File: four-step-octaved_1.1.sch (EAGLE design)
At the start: 39 parts, among them IC1 556, IC2 4017N, IC3 4040N, J1 -BATTERY+, J2 SPEAKER, U1 LM386N

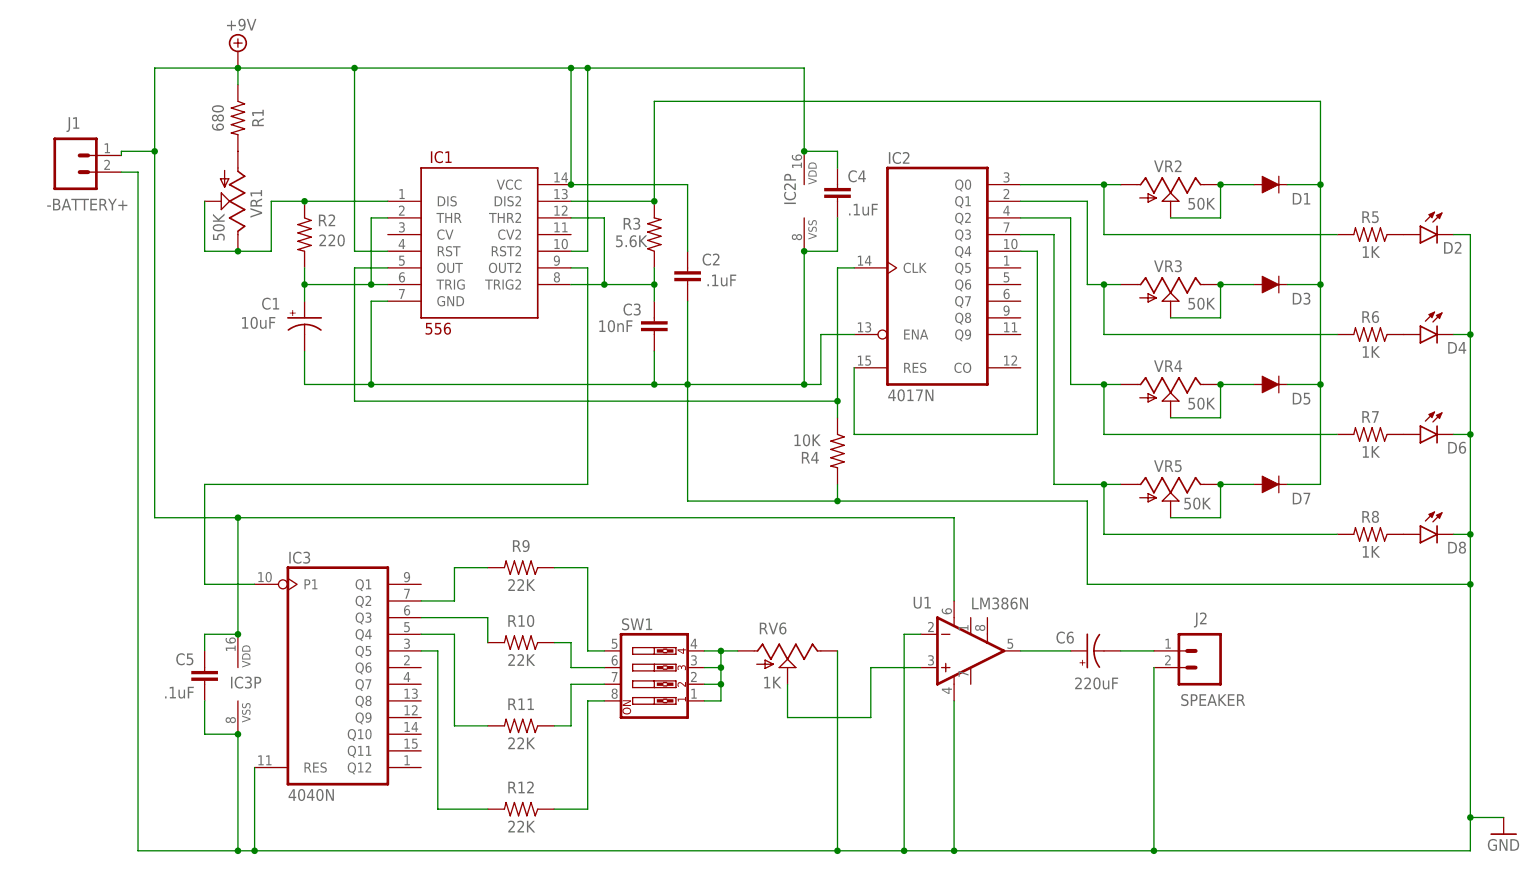
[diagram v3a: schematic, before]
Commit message: Add switch
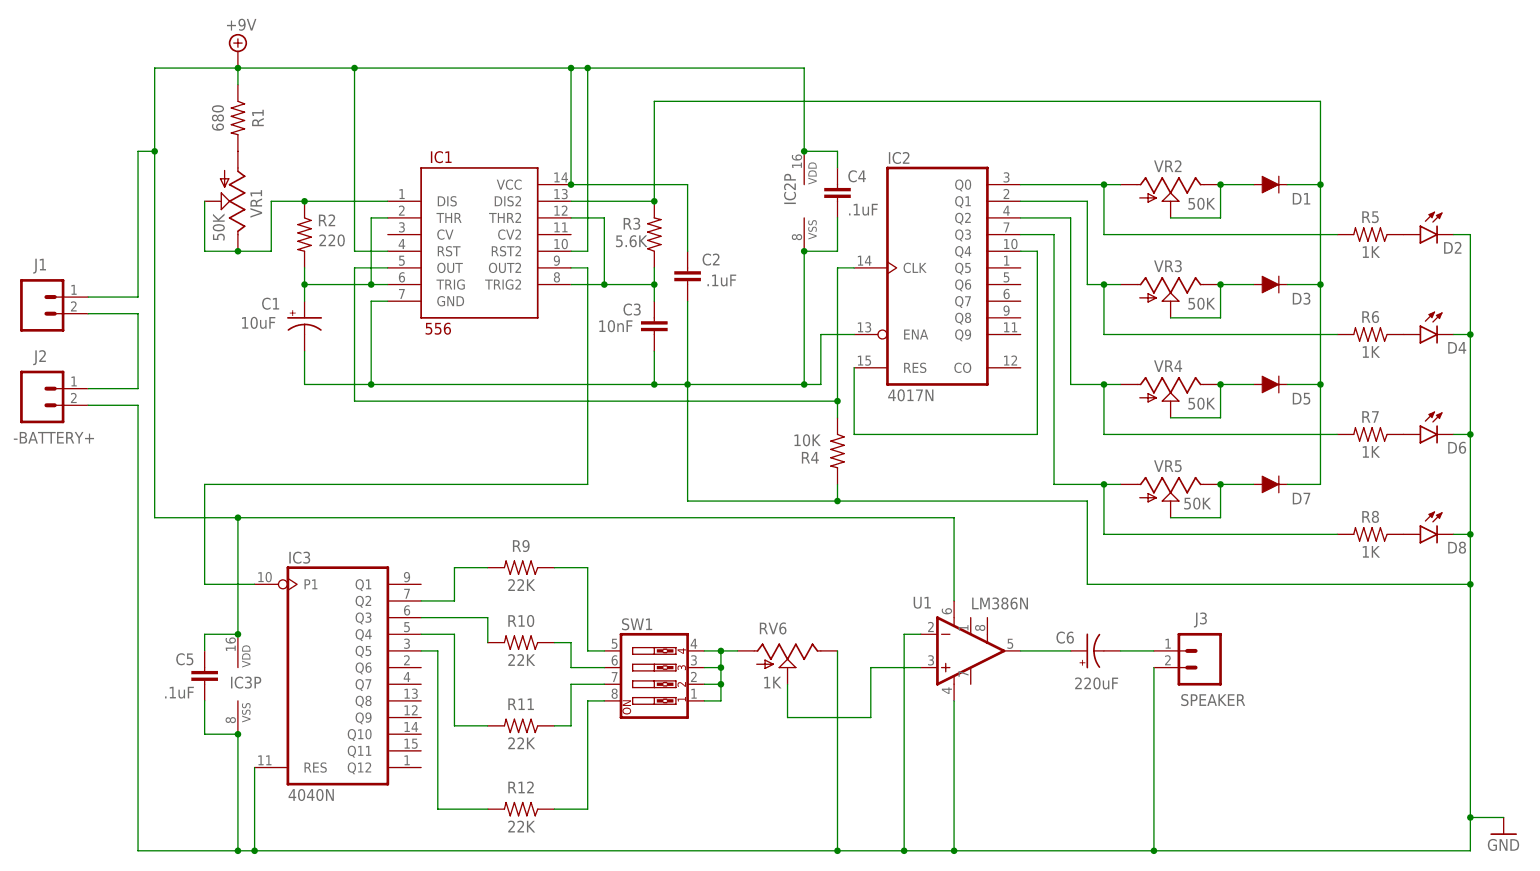
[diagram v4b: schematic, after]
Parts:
- added J3: SPEAKER, SparkFun-Connectors:CONN_02
- J1: value -BATTERY+ -> (none)
- J2: value SPEAKER -> -BATTERY+
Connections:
- new net N$32: J1.2, J2.1
- net GND: now also J3.2; no longer J1.2
- net N$27: now also J3.1; no longer J2.1
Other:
- moved on the sheet: J1, J2
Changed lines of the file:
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@@
 <setting verticaltext="up"/>
 </settings>
-<grid distance="0.1" unitdist="inch" unit="inch" style="lines" multiple="1" display="no" altdistance="0.01" altunitdist="inch" altunit="inch"/>
+<grid distance="0.025" unitdist="inch" unit="inch" style="lines" multiple="1" display="no" altdistance="0.01" altunitdist="inch" altunit="inch"/>
 <layers>
 <layer number="1" name="Top" color="4" fill="1" visible="no" active="no"/>
@@
 <part name="C5" library="SparkFun-Capacitors" deviceset="0.1UF" device="-KIT-EZ-50V-20%" value=".1uF"/>
 <part name="C6" library="SparkFun-Capacitors" deviceset="100UF-POLAR" device="-RADIAL-2.5MM-25V-20%" value="220uF"/>
-<part name="J2" library="SparkFun-Connectors" deviceset="CONN_02" device="" value="SPEAKER"/>
-<part name="J1" library="SparkFun-Connectors" deviceset="CONN_02" device="" value="-BATTERY+"/>
+<part name="J3" library="SparkFun-Connectors" deviceset="CONN_02" device="" value="SPEAKER"/>
+<part name="J2" library="SparkFun-Connectors" deviceset="CONN_02" device="" value="-BATTERY+"/>
 <part name="R11" library="SparkFun-Resistors" deviceset="1KOHM" device="-HORIZ-1/4W-1%" value="22K"/>
 <part name="R12" library="SparkFun-Resistors" deviceset="1KOHM" device="-HORIZ-1/4W-1%" value="22K"/>
 <part name="SW1" library="special" deviceset="SW_DIP-4" device=""/>
+<part name="J1" library="SparkFun-Connectors" deviceset="CONN_02" device=""/>
 </parts>
 <sheets>
@@
 <attribute name="VALUE" x="108.966" y="13.716" size="1.778" layer="96" font="vector" rot="R180"/>
 </instance>
-<instance part="J2" gate="G$1" x="121.92" y="17.78" smashed="yes" rot="R180">
+<instance part="J3" gate="G$1" x="121.92" y="17.78" smashed="yes" rot="R180">
 <attribute name="VALUE" x="128.27" y="11.176" size="1.778" layer="96" font="vector" rot="R180"/>
 <attribute name="NAME" x="122.555" y="23.622" size="1.778" layer="95" font="vector" rot="R180"/>
 </instance>
-<instance part="J1" gate="G$1" x="-50.8" y="93.345" smashed="yes" rot="MR180">
-<attribute name="VALUE" x="-54.61" y="86.741" size="1.778" layer="96" font="vector" rot="MR180"/>
-<attribute name="NAME" x="-51.435" y="99.187" size="1.778" layer="95" font="vector" rot="MR180"/>
+<instance part="J2" gate="G$1" x="-55.88" y="57.785" smashed="yes" rot="MR180">
+<attribute name="VALUE" x="-59.69" y="51.181" size="1.778" layer="96" font="vector" rot="MR180"/>
+<attribute name="NAME" x="-56.515" y="63.627" size="1.778" layer="95" font="vector" rot="MR180"/>
 </instance>
 <instance part="R11" gate="G$1" x="17.78" y="6.35" smashed="yes" rot="R180">
@@
 </instance>
 <instance part="SW1" gate="A" x="38.1" y="15.24"/>
+<instance part="J1" gate="G$1" x="-55.88" y="71.755" smashed="yes" rot="MR180">
+<attribute name="VALUE" x="-59.69" y="65.151" size="1.778" layer="96" font="vector" rot="MR180"/>
+<attribute name="NAME" x="-56.515" y="77.597" size="1.778" layer="95" font="vector" rot="MR180"/>
+</instance>
 </instances>
 <busses>
@@
 <wire x1="-30.48" y1="20.32" x2="-30.48" y2="17.78" width="0.1524" layer="91"/>
 <wire x1="-38.1" y1="106.68" x2="-38.1" y2="93.98" width="0.1524" layer="91"/>
-<pinref part="J1" gate="G$1" pin="1"/>
 <wire x1="-38.1" y1="93.98" x2="-38.1" y2="38.1" width="0.1524" layer="91"/>
-<wire x1="-38.1" y1="93.98" x2="-43.18" y2="93.98" width="0.1524" layer="91"/>
-<wire x1="-43.18" y1="93.98" x2="-43.18" y2="93.345" width="0.1524" layer="91"/>
+<wire x1="-38.1" y1="93.98" x2="-40.64" y2="93.98" width="0.1524" layer="91"/>
 <junction x="-38.1" y="93.98"/>
 <pinref part="IC1" gate="G$1" pin="RST2"/>
@@
 <wire x1="27.94" y1="78.74" x2="27.94" y2="106.68" width="0.1524" layer="91"/>
 <junction x="27.94" y="106.68"/>
+<pinref part="J1" gate="G$1" pin="1"/>
+<wire x1="-48.26" y1="71.755" x2="-40.64" y2="71.755" width="0.1524" layer="91"/>
+<wire x1="-40.64" y1="71.755" x2="-40.64" y2="93.98" width="0.1524" layer="91"/>
 </segment>
 </net>
@@
 <segment>
 <pinref part="C6" gate="G$1" pin="-"/>
-<pinref part="J2" gate="G$1" pin="1"/>
+<pinref part="J3" gate="G$1" pin="1"/>
 <wire x1="114.3" y1="17.78" x2="109.22" y2="17.78" width="0.1524" layer="91"/>
 </segment>
@@
 <wire x1="76.2" y1="-12.7" x2="83.82" y2="-12.7" width="0.1524" layer="91"/>
 <junction x="76.2" y="-12.7"/>
-<pinref part="J2" gate="G$1" pin="2"/>
+<pinref part="J3" gate="G$1" pin="2"/>
 <wire x1="114.3" y1="-12.7" x2="114.3" y2="15.24" width="0.1524" layer="91"/>
 <wire x1="83.82" y1="-12.7" x2="114.3" y2="-12.7" width="0.1524" layer="91"/>
@@
 <wire x1="104.14" y1="27.94" x2="104.14" y2="40.64" width="0.1524" layer="91"/>
 <junction x="162.56" y="27.94"/>
-<pinref part="J1" gate="G$1" pin="2"/>
-<wire x1="-43.18" y1="90.805" x2="-40.64" y2="90.805" width="0.1524" layer="91"/>
-<wire x1="-40.64" y1="90.805" x2="-40.64" y2="-12.7" width="0.1524" layer="91"/>
+<pinref part="J2" gate="G$1" pin="2"/>
+<wire x1="-48.26" y1="55.245" x2="-40.64" y2="55.245" width="0.1524" layer="91"/>
+<wire x1="-40.64" y1="55.245" x2="-40.64" y2="-12.7" width="0.1524" layer="91"/>
 <wire x1="-40.64" y1="-12.7" x2="-25.4" y2="-12.7" width="0.1524" layer="91"/>
 <junction x="-25.4" y="-12.7"/>
@@
 </segment>
 </net>
+<net name="N$32" class="0">
+<segment>
+<pinref part="J1" gate="G$1" pin="2"/>
+<wire x1="-48.26" y1="69.215" x2="-40.64" y2="69.215" width="0.1524" layer="91"/>
+<wire x1="-40.64" y1="69.215" x2="-40.64" y2="57.785" width="0.1524" layer="91"/>
+<pinref part="J2" gate="G$1" pin="1"/>
+<wire x1="-40.64" y1="57.785" x2="-48.26" y2="57.785" width="0.1524" layer="91"/>
+</segment>
+</net>

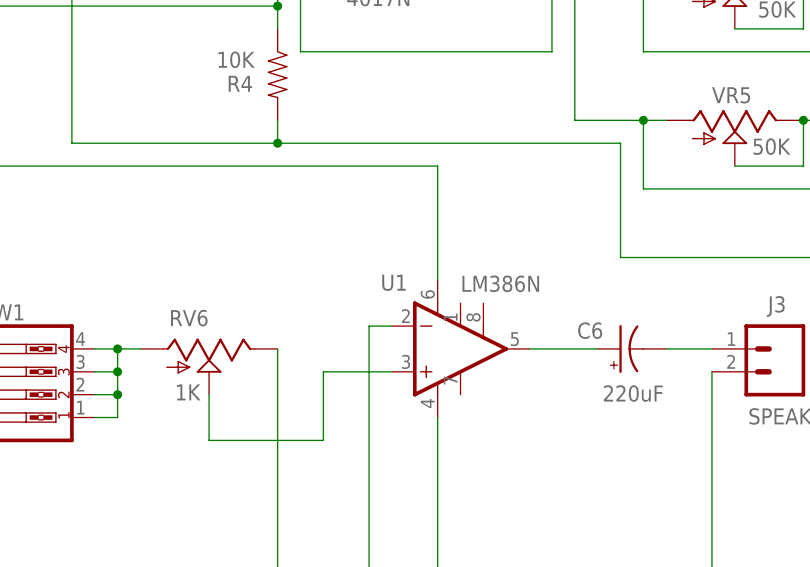
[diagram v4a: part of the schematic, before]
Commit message: Update 386 name
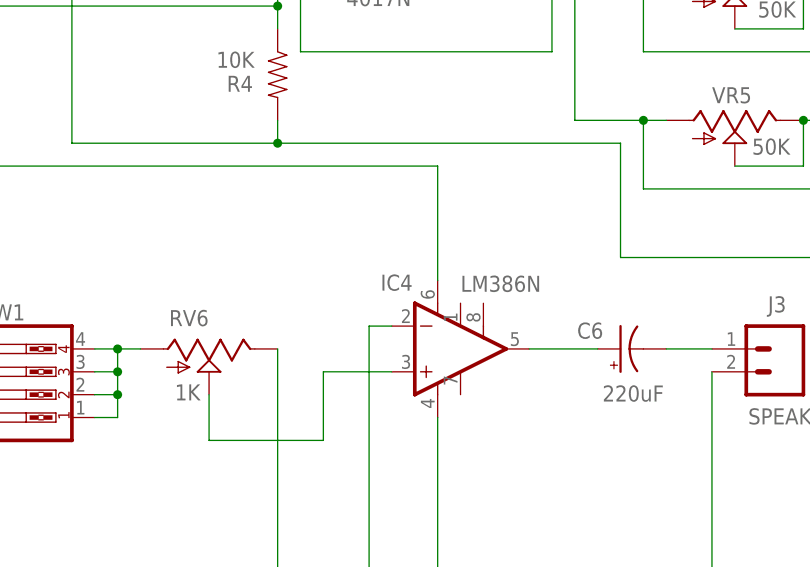
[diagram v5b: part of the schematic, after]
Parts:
- renumbered U1 to IC4
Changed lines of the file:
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@@
 <part name="IC2" library="40xx" deviceset="4017" device="N"/>
 <part name="IC3" library="40xx" deviceset="4040" device="N"/>
-<part name="U1" library="SparkFun-IC-Amplifiers" deviceset="LM386" device="" value="LM386N"/>
+<part name="IC4" library="SparkFun-IC-Amplifiers" deviceset="LM386" device="" value="LM386N"/>
 <part name="SUPPLY1" library="supply2" deviceset="+9V" device=""/>
 <part name="GND1" library="supply1" deviceset="GND" device=""/>
@@
 <instance part="IC2" gate="A" x="81.28" y="76.2"/>
 <instance part="IC3" gate="A" x="-10.16" y="15.24"/>
-<instance part="U1" gate="G1" x="83.82" y="17.78" smashed="yes">
+<instance part="IC4" gate="G1" x="83.82" y="17.78" smashed="yes">
 <attribute name="NAME" x="77.47" y="24.257" size="1.778" layer="95" font="vector"/>
 <attribute name="VALUE" x="86.36" y="24.13" size="1.778" layer="95" font="vector"/>
@@
 <pinref part="IC3" gate="P" pin="VDD"/>
 <junction x="-25.4" y="20.32"/>
-<pinref part="U1" gate="G1" pin="V+"/>
+<pinref part="IC4" gate="G1" pin="V+"/>
 <wire x1="83.82" y1="25.4" x2="83.82" y2="38.1" width="0.1524" layer="91"/>
 <wire x1="83.82" y1="38.1" x2="-25.4" y2="38.1" width="0.1524" layer="91"/>
@@
 <pinref part="RV6" gate="G$1" pin="S"/>
 <wire x1="58.42" y1="12.7" x2="58.42" y2="7.62" width="0.1524" layer="91"/>
-<pinref part="U1" gate="G1" pin="+IN"/>
+<pinref part="IC4" gate="G1" pin="+IN"/>
 <wire x1="58.42" y1="7.62" x2="71.12" y2="7.62" width="0.1524" layer="91"/>
 <wire x1="71.12" y1="7.62" x2="71.12" y2="15.24" width="0.1524" layer="91"/>
@@
 <segment>
 <pinref part="C6" gate="G$1" pin="+"/>
-<pinref part="U1" gate="G1" pin="OUT"/>
+<pinref part="IC4" gate="G1" pin="OUT"/>
 <wire x1="101.6" y1="17.78" x2="93.98" y2="17.78" width="0.1524" layer="91"/>
 </segment>
@@
 <wire x1="-22.86" y1="-12.7" x2="66.04" y2="-12.7" width="0.1524" layer="91"/>
 <junction x="-22.86" y="-12.7"/>
-<pinref part="U1" gate="G1" pin="-IN"/>
+<pinref part="IC4" gate="G1" pin="-IN"/>
 <wire x1="78.74" y1="20.32" x2="76.2" y2="20.32" width="0.1524" layer="91"/>
 <wire x1="76.2" y1="20.32" x2="76.2" y2="-12.7" width="0.1524" layer="91"/>
 <wire x1="66.04" y1="-12.7" x2="76.2" y2="-12.7" width="0.1524" layer="91"/>
 <junction x="66.04" y="-12.7"/>
-<pinref part="U1" gate="G1" pin="V-"/>
+<pinref part="IC4" gate="G1" pin="V-"/>
 <wire x1="83.82" y1="10.16" x2="83.82" y2="-12.7" width="0.1524" layer="91"/>
 <wire x1="76.2" y1="-12.7" x2="83.82" y2="-12.7" width="0.1524" layer="91"/>

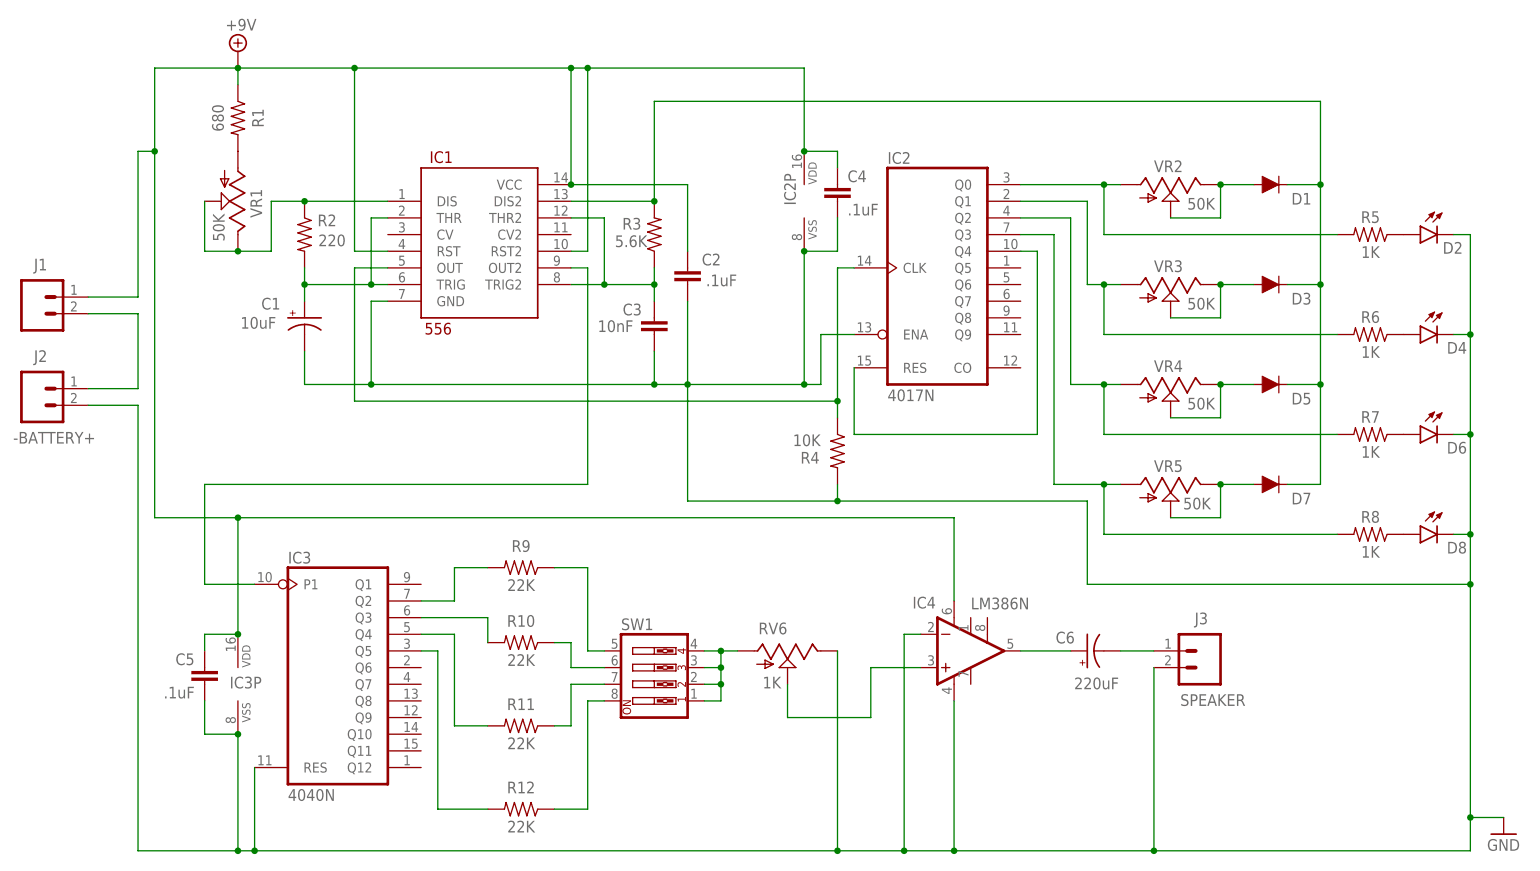
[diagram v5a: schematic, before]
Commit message: Update to 1.1.2
- Add header label text
- Indicate battery and speaker polarity
- Reverse order octave switches: low to high = left to right
- Label ICs
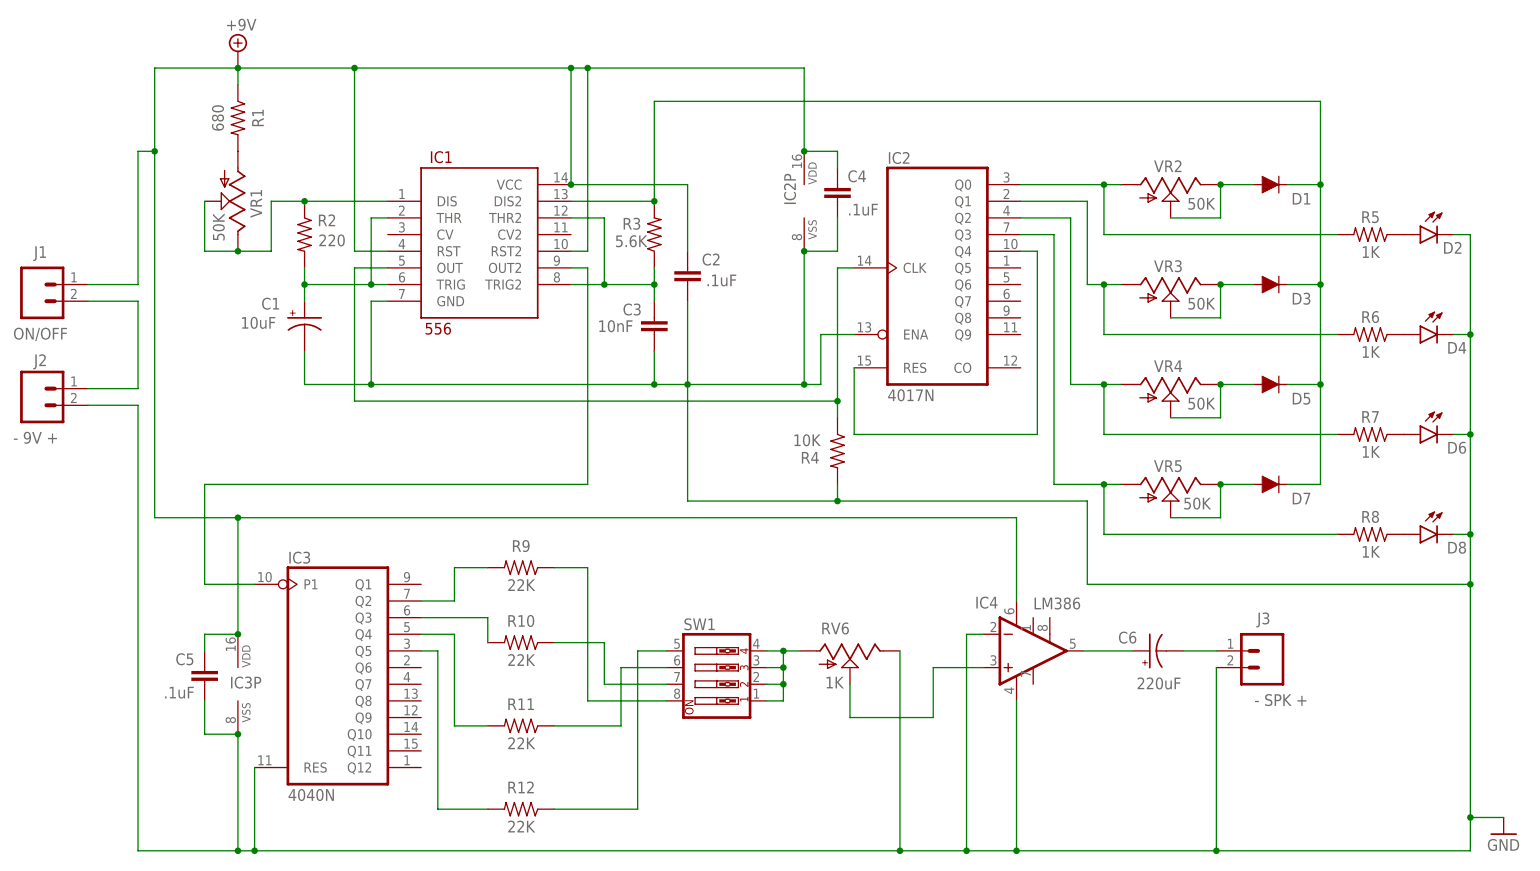
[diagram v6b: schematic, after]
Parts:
- C6: device SparkFun-Capacitors:100UF-POLAR-RADIAL-2.5MM-25V-20% -> SparkFun-Capacitors:10UF-POLAR-RADIAL-2.5MM-25V-20%
- IC4: value LM386N -> LM386
- J1: value (none) -> ON/OFF
- J2: value -BATTERY+ -> - 9V +
- J3: value SPEAKER -> - SPK +
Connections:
- net N$23: now also R12.1, SW1.5; no longer R10.1, SW1.6
- net N$26: now also SW1.6; no longer SW1.7
- net N$29: now also R10.1, SW1.7; no longer R9.1, SW1.5
- net N$30: now also R9.1; no longer R12.1
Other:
- moved on the sheet: C6, IC4, J1, J3, RV6, SW1
